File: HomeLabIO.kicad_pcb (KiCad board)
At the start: 4 copper layers, 230 x 42 mm, 77 parts, among them J1 104031-0811, J2 HDMI_A, J3 Bus_M.2_Socket_M, J5 61900419521, J6 USB_C_Receptacle_USB2.0_16P, M2 CM4-GPIO, U1 MagJack-A70-112-331N126, U10 AP62301WU-7, U11 EMC2301, U12 FT234XD-R, U13 TPD4EUSB30, U2 TPD4EUSB30, U3 TPD4EUSB30, U4 RT9742GGJ5, U5 74LVC1G07SE-7, U7 AG5405

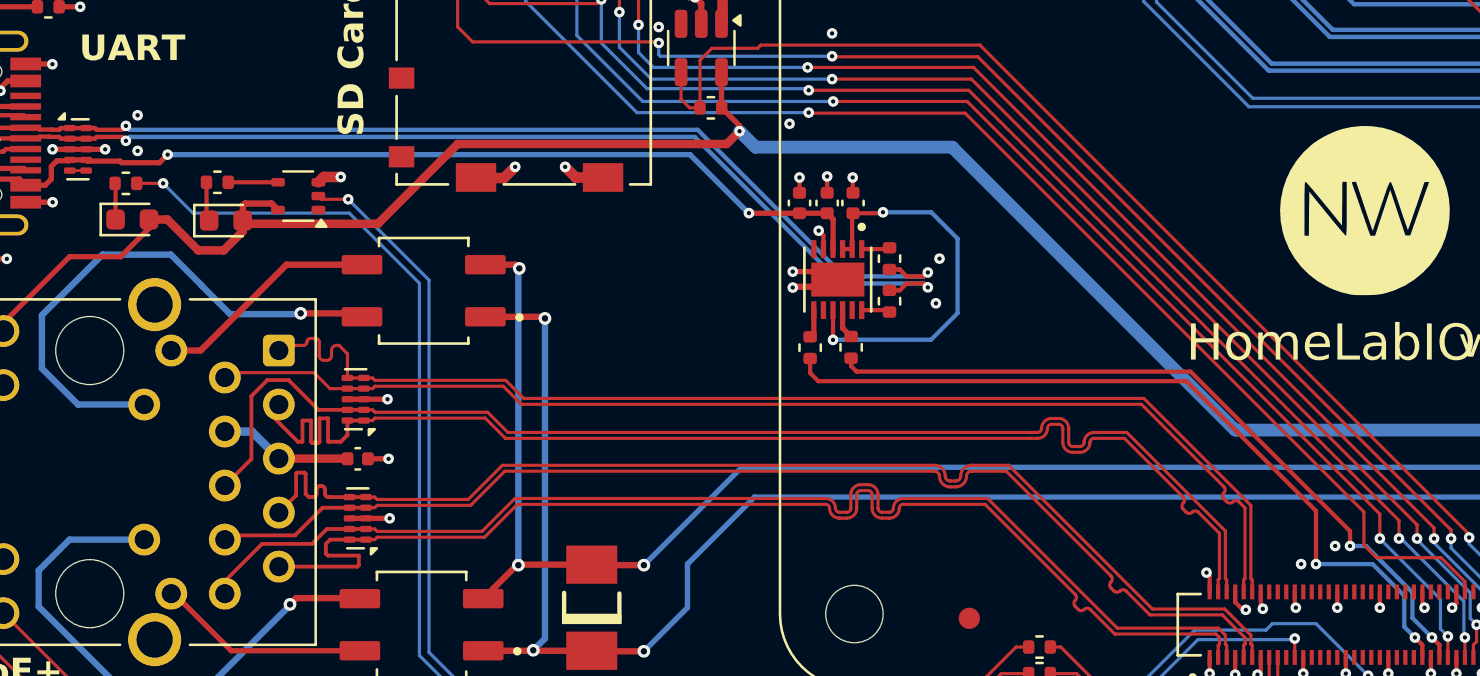
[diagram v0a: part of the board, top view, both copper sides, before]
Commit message: fix: BOM issues and FTDI wiring (#2)
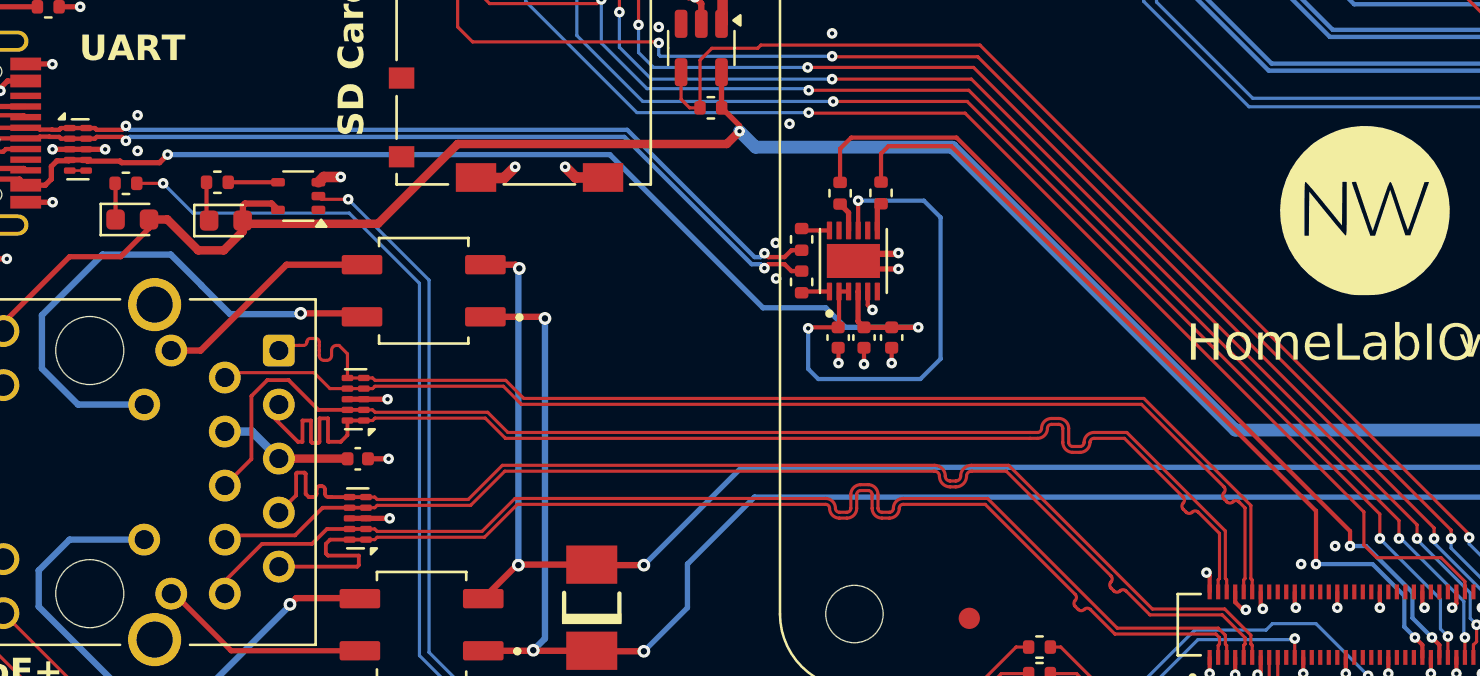
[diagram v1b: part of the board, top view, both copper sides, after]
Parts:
- moved R9 8.00 mm to (72.8, 82.3), turned to -90 degrees
- moved C16 7.67 mm to (73.3, 89.1), turned to -90 degrees
- moved R10 7.26 mm to (70.9, 82.3), turned to -90 degrees
- moved C15 6.56 mm to (72.0, 89.1), turned to -90 degrees
- moved C14 6.36 mm to (70.8, 89.1), turned to -90 degrees
- moved R12 5.05 mm to (69.1, 84.5), turned to -90 degrees
- moved R11 4.28 mm to (69.1, 86.5), turned to 90 degrees
- moved U12 1.14 mm to (71.5, 85.5), turned to 90 degrees
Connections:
- R11 pad 2: /USB/FTDI_USB_P -> /USB/FTDI_USB_N
- R12 pad 2: /USB/FTDI_USB_N -> /USB/FTDI_USB_P
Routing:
- net /USB/VBus_Slave: track 51.8 -> 60.9 mm
- net /USB/FTDI_USB_P: track 53.3 -> 45.2 mm
- net /USB/FTDI_USB_N: track 53.3 -> 45.2 mm
- net /CM4_GPIO/UART.TX: track 35.2 -> 41.6 mm
- net Net-(U12-3V3OUT): track 18.8 -> 24.5 mm
- net /CM4_GPIO/UART.RX: track 37.7 -> 39.6 mm

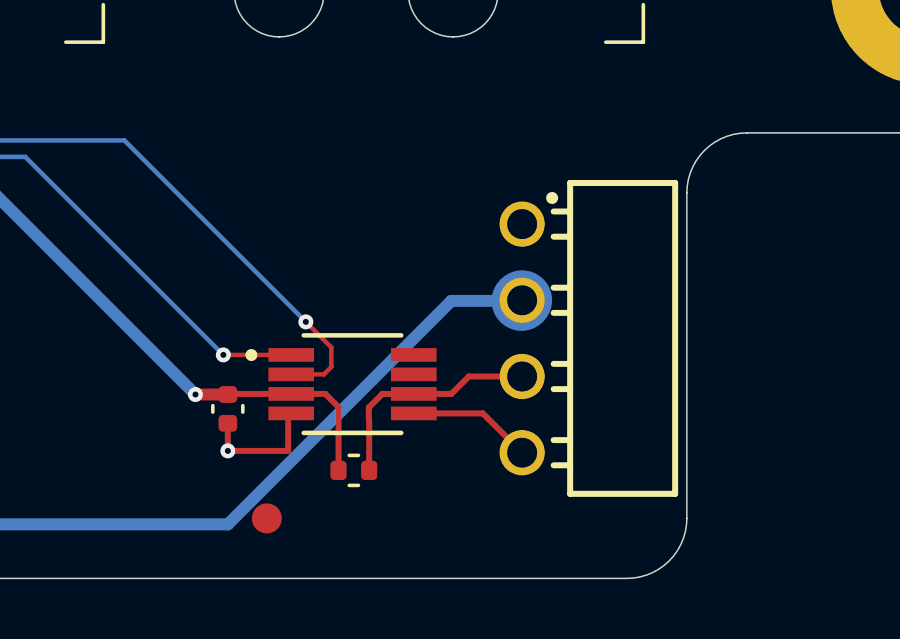
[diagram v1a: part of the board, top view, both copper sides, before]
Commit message: fix: move fan pins to board edge (#4)
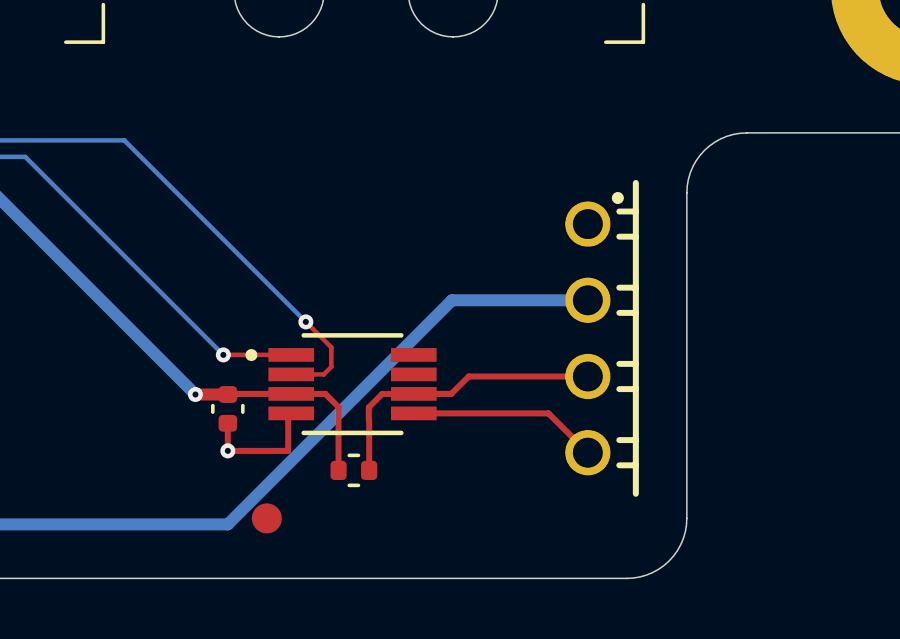
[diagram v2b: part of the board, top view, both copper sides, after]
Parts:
- moved J5 2.19 mm to (229.2, 98.6)
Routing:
- net Net-(U11-TACH): track 7.64 -> 9.83 mm
- net Net-(U11-PWM): track 4.05 -> 6.24 mm
- net +5V: track 167.8 -> 170.0 mm

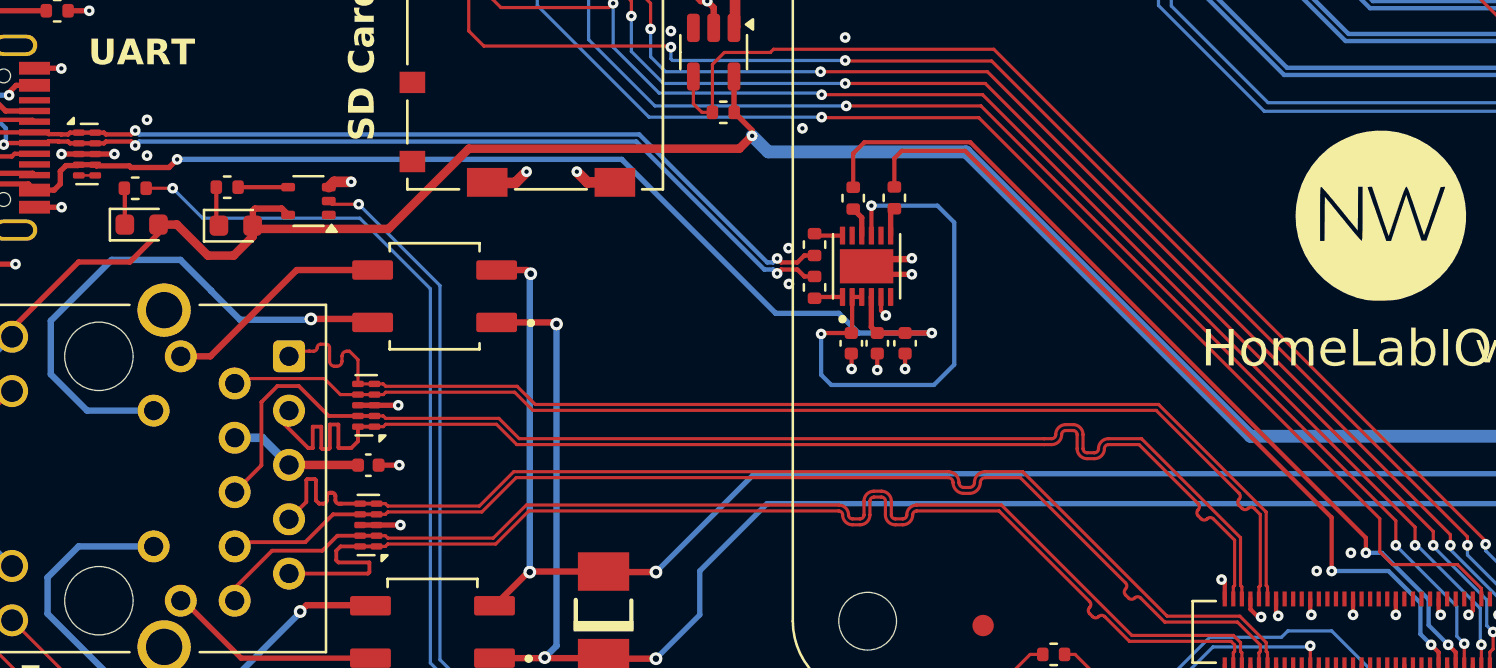
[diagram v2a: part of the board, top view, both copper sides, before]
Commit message: feat: switch UART chipset
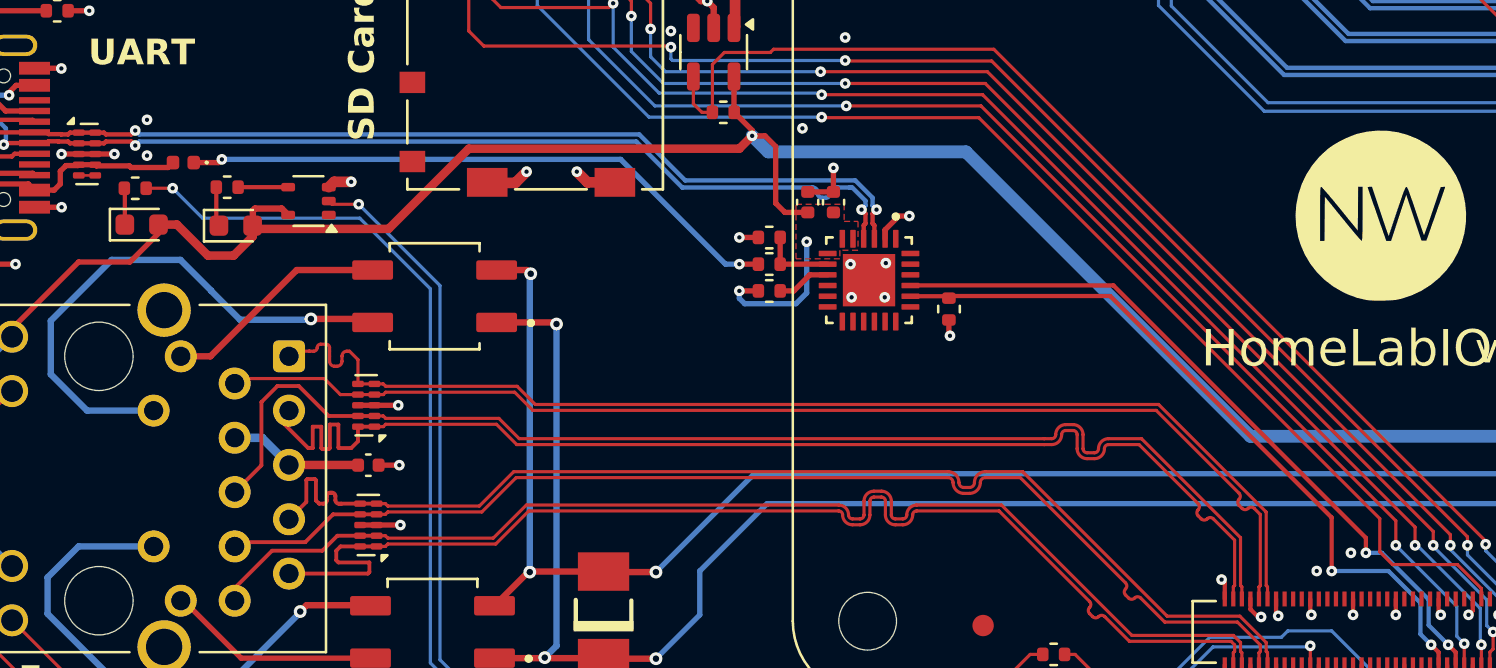
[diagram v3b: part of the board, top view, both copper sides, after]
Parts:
- removed C14, C15, C16: 100n, Capacitor_SMD:C_0402_1005Metric
- removed R10: 220, Resistor_SMD:R_0402_1005Metric
- removed R11, R12: 22, Resistor_SMD:R_0402_1005Metric
- removed U12: FT234XD-R, HomeLabIO:SON45P300X300X80-13N
- added C3: 100n, Capacitor_SMD:C_0402_1005Metric, F.Cu at (70.0, 82.5)
- added C4: 4u7, Capacitor_SMD:C_0402_1005Metric, F.Cu at (68.8, 82.5)
- added D4: D_Schottky_Small, Diode_SMD:D_0402_1005Metric, F.Cu at (39.5, 80.7)
- added R15: 1k, Resistor_SMD:R_0402_1005Metric, F.Cu at (67.0, 86.7)
- added R16: 22.1k, Resistor_SMD:R_0402_1005Metric, F.Cu at (67.0, 85.4)
- added R17: 47.5k, Resistor_SMD:R_0402_1005Metric, F.Cu at (67.0, 84.2)
- added U6: CP2102N-A02-GQFN24R, HomeLabIO:QFN50P400X400X80-25N, F.Cu at (71.6, 86.2)
- R9: value 220 -> 10k
- moved R9 5.79 mm to (75.3, 87.5)
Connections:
- net /USB/VBus_Slave renamed /USB/VBUS
- R9 pad 2: Net-(U12-TXD) -> GND
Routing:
- net /USB/VBUS: track 60.9 -> 17.6 mm, vias 4 -> 2
- net /USB/VBus_UART: track 0.00 -> 28.5 mm, vias 0 -> 2
- net Net-(U12-3V3OUT): track 24.5 -> 0.00 mm, vias 2 -> 0
- net +3.3V: track 232.8 -> 245.5 mm, vias 4 -> 6
- net /CM4_GPIO/UART.TX: track 41.6 -> 34.3 mm
- net /CM4_GPIO/UART.RX: track 39.6 -> 34.6 mm
- net Net-(U6-VBUS): track 0.00 -> 3.47 mm
- net /USB/FTDI_USB_P: track 45.2 -> 48.5 mm
- net /USB/FTDI_USB_N: track 45.2 -> 48.4 mm
- net Net-(U6-~{RST}): track 0.00 -> 2.53 mm
- net Net-(U12-RXD): track 1.41 -> 0.00 mm
- net Net-(U12-USBDP): track 1.34 -> 0.00 mm
- net Net-(U12-USBDM): track 1.33 -> 0.00 mm
- net Net-(U12-TXD): track 1.33 -> 0.00 mm

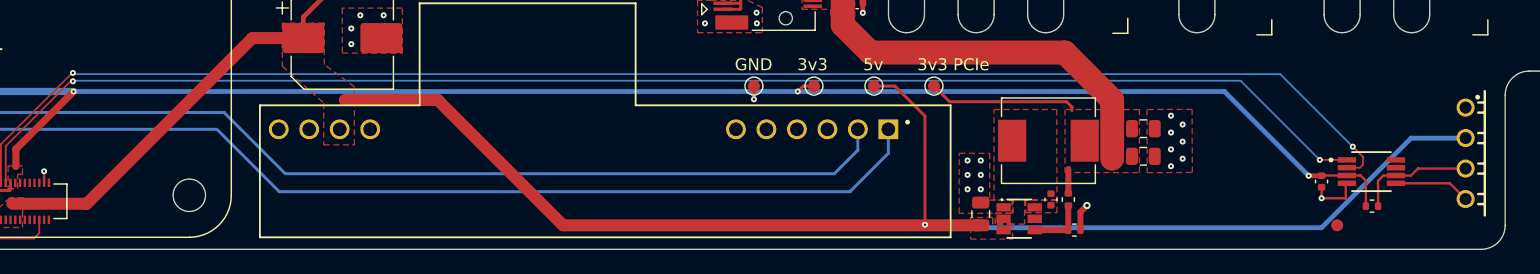
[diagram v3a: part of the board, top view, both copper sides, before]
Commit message: feat: move fan driver to be more compact (#6)
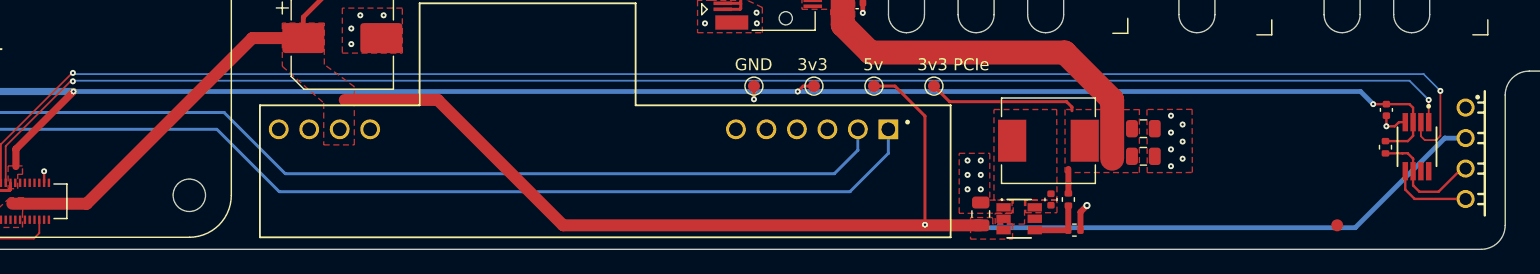
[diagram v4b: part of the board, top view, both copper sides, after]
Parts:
- moved C2 8.05 mm to (219.3, 95.0)
- moved R8 5.03 mm to (219.2, 98.1), turned to -90 degrees
- moved U11 4.33 mm to (221.8, 98.0), turned to -90 degrees
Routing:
- net /CM4_GPIO/SCL: track 124.3 -> 133.2 mm
- net /CM4_GPIO/SDA: track 119.7 -> 126.3 mm
- net +3.3V: track 245.5 -> 249.6 mm
- net GND: track 133.2 -> 131.6 mm
- net Net-(U11-PWM): track 6.24 -> 6.88 mm

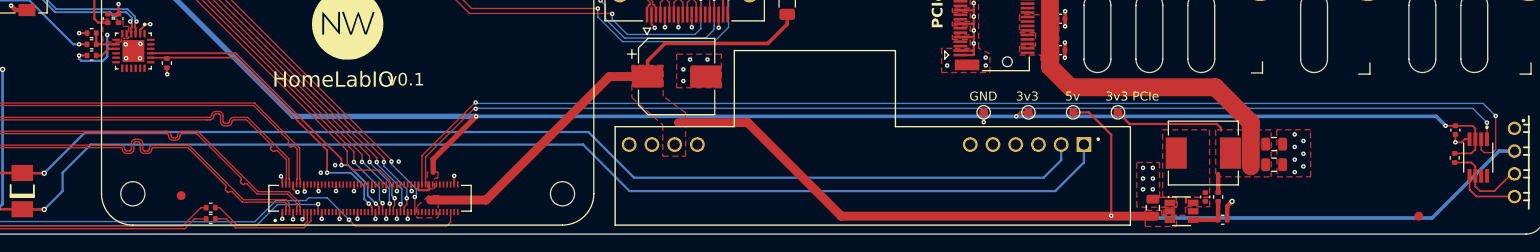
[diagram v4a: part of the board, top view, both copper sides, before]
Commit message: feat: add UART activity LEDs (#7)
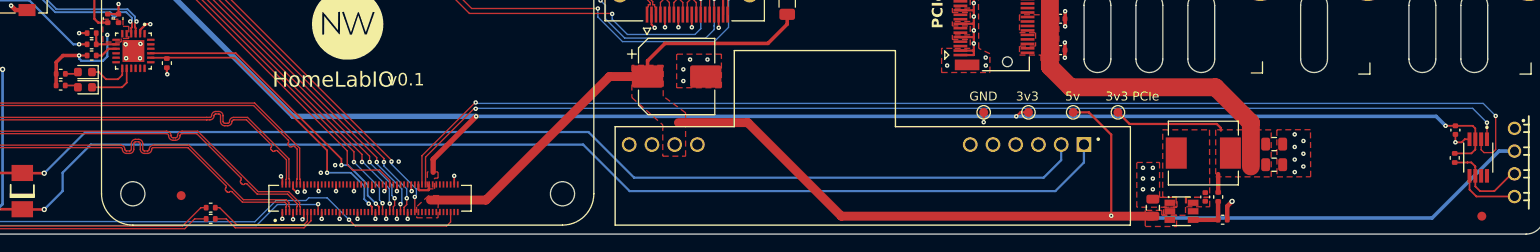
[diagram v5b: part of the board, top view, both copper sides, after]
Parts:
- added D5: LED, LED_SMD:LED_0603_1608Metric, F.Cu at (66.2, 90.2)
- added D6: LED, LED_SMD:LED_0603_1608Metric, F.Cu at (66.2, 88.5)
- added R10: 1k, Resistor_SMD:R_0402_1005Metric, F.Cu at (63.5, 90.0)
- added R11: 1k, Resistor_SMD:R_0402_1005Metric, F.Cu at (63.5, 88.7)
- moved FID1 7.05 mm to (222.2, 104.6)
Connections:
- U6 pad 13: unconnected-(U6-GPIO.1/RXT-Pad13) -> Net-(D6-K)
- U6 pad 14: unconnected-(U6-GPIO.0/TXT-Pad14) -> Net-(D5-K)
- U6 pad 20: /CM4_GPIO/UART.RX -> /CM4_GPIO/UART.TX
- U6 pad 21: /CM4_GPIO/UART.TX -> /CM4_GPIO/UART.RX
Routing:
- net Net-(D5-K): track 0.00 -> 5.69 mm
- net +3.3V: track 249.6 -> 255.1 mm
- net Net-(D6-K): track 0.00 -> 4.65 mm
- net Net-(D5-A): track 0.00 -> 1.50 mm
- net Net-(D6-A): track 0.00 -> 1.49 mm
